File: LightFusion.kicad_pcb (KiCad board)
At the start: 4 copper layers, 52.3 x 52.3 mm, 100 parts, among them J1 303C-C4115-30-04, J2 TC2030-IDC-FP, P1 PHR-2, U1 MDBT42-512KV2, U10 OPA381AIDGKR, U2 TPS7A2033PDBVR, U3 TPS22918DBVR, U4 DRV8837DSGR, U5 ADS1292IPBSR, U6 STCS1APHR_FIXED, U7 STCS1APHR_FIXED, U8 TMP1075NDRLR, U9 MCP3561T-E_ST

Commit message: new rect version
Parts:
- removed C30, C31: 10 nF, LightFusion:C_0603_1608Metric
- added OPT1: FP11055_LISA2-RS-PIN, LightFusion:LEDIL_FP11055_LISA2_RS_PIN, F.Cu at (141.9, 130.2)
- added OPT2: FP11055_LISA2-RS-PIN, LightFusion:LEDIL_FP11055_LISA2_RS_PIN, F.Cu at (154.0, 130.2)
- added R36: 100k, LightFusion:R_0603_1608Metric, F.Cu at (154.1, 125.6)
- added R37: 100k, LightFusion:R_1206_3216Metric, F.Cu at (134.3, 125.0)
- C26, C28: value 4.7 uF -> 10 uF
- E1, E2, E3, E4, E5: footprint LightFusion:MILL-MAX_0906-0-15-20-76-14-11-0 -> LightFusion:0914015207714110
- J2: footprint LightFusion:TC2030IDCNL -> LightFusion:TC2030IDCFP
- U3: footprint LightFusion:TPS22918DBVR-6N -> LightFusion:TPS22918DBVT
- U6, U7: value STCS1APHR_FIXED -> ~; footprint LightFusion:STCS1APHR-8_STM -> LightFusion:PAM2808BLBR
- moved R25 1.55 mm to (135.1, 121.0)
- moved C26 0.18 mm to (127.3, 132.0)
- moved J2 0.15 mm to (137.9, 147.1)
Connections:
- D1 pad 1: /LED/LED730_K -> Net-(D1-K)
- D1 pad 2: VBAT_SYSTEM -> Net-(D1-A)
- D2 pad 1: /LED/LED850_K -> Net-(D2-K)
- D2 pad 2: VBAT_SYSTEM -> Net-(D2-A)
- R25 pad 1: Net-(U6-FB) -> Net-(D1-K)
- R26 pad 1: Net-(U7-FB) -> Net-(D2-K)
- U6 pad 1: VBAT_SYSTEM -> unconnected-(U6-NC-Pad1)
- U6 pad 2: PWM_730 -> VBAT_SYSTEM
- U6 pad 3: 3V3_DIG -> PWM_730
- U6 pad 4: /LED/LED730_K -> GND
- U6 pad 5: Net-(U6-FB) -> unconnected-(U6-NC-Pad5)
- U6 pad 6: GND -> Net-(D1-K)
- U6 pad 7: Net-(U6-SLOPE) -> Net-(D1-A)
- U7 pad 1: VBAT_SYSTEM -> unconnected-(U7-NC-Pad1)
- U7 pad 2: PWM_850 -> VBAT_SYSTEM
- U7 pad 3: 3V3_DIG -> PWM_850
- U7 pad 4: /LED/LED850_K -> GND
- U7 pad 5: Net-(U7-FB) -> unconnected-(U7-NC-Pad5)
- U7 pad 6: GND -> Net-(D2-K)
- U7 pad 7: Net-(U7-SLOPE) -> Net-(D2-A)
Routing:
- net 3V3_DIG: track 174.2 -> 0.00 mm, vias 19 -> 0
- net GND: track 130.1 -> 0.00 mm, vias 70 -> 0
- net VBAT_SYSTEM: track 110.3 -> 0.00 mm, vias 5 -> 0
- net /SWDIO: track 84.8 -> 0.00 mm, vias 2 -> 0
- net /SWDCLK: track 83.5 -> 0.00 mm, vias 4 -> 0
- net /RESET: track 79.4 -> 0.00 mm, vias 2 -> 0
- net ADC_MOSI: track 56.7 -> 0.00 mm, vias 4 -> 0
- net /MCU_STIM_IN2: track 55.8 -> 0.00 mm, vias 2 -> 0
- net ADC_MISO: track 54.4 -> 0.00 mm, vias 3 -> 0
- net ADC_SCK: track 54.4 -> 0.00 mm, vias 4 -> 0
- net /MCU_STIM_IN1: track 50.0 -> 0.00 mm, vias 2 -> 0
- net PWM_730: track 44.2 -> 0.00 mm
- net ADC_DRDY_N: track 41.3 -> 0.00 mm, vias 2 -> 0
- net /PD_ADC/3V3_A: track 40.5 -> 0.00 mm, vias 2 -> 0
- net /MCU_STIM_EN: track 40.3 -> 0.00 mm, vias 2 -> 0
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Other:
- board size 52.3 x 52.3 mm -> 61 x 52.3 mm

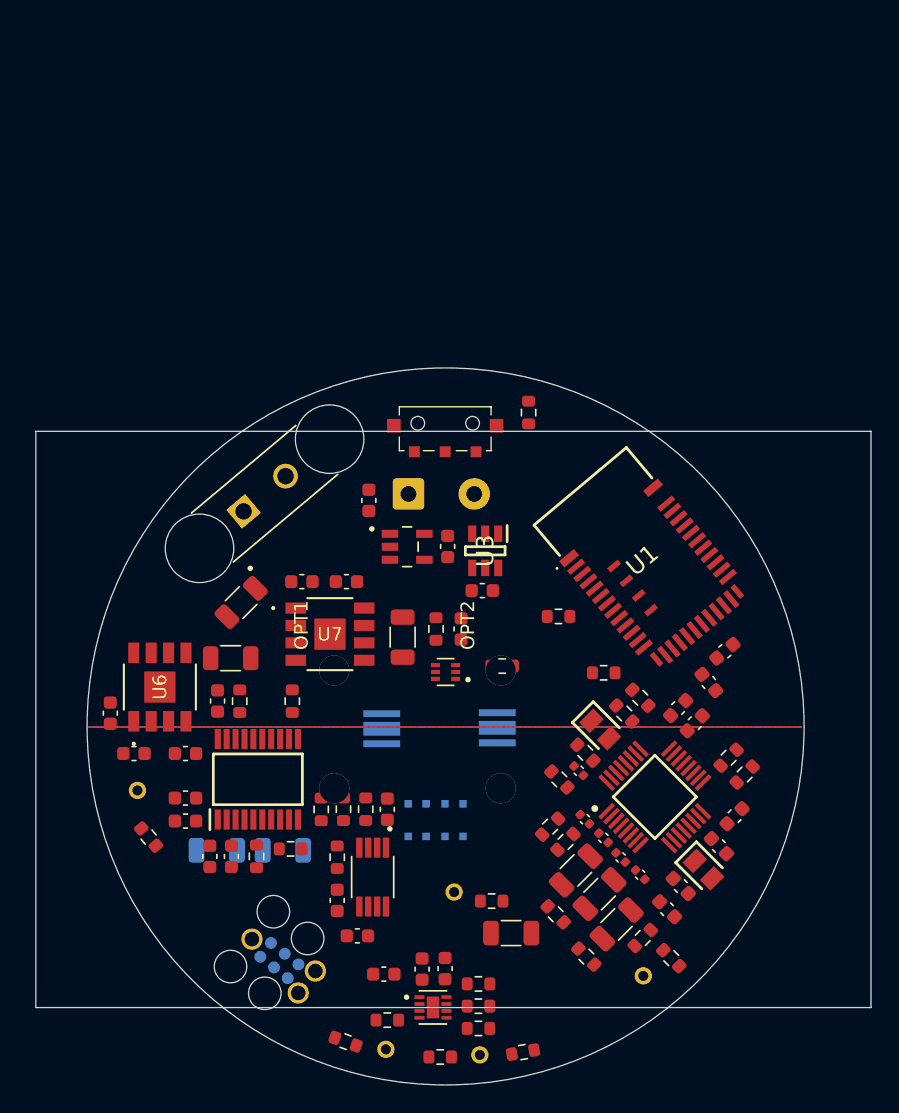
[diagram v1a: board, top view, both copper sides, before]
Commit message: rectangle placement
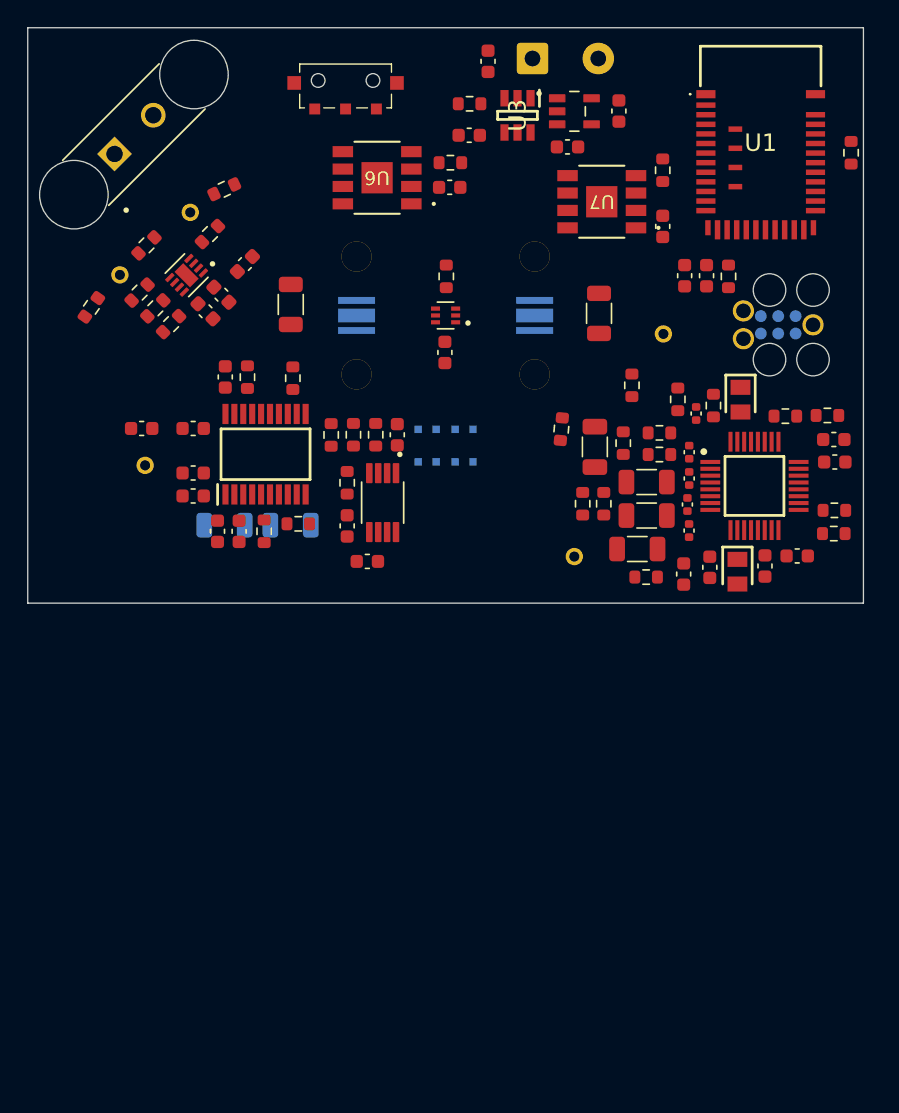
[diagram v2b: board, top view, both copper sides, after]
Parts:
- OPT1, OPT2: moved to B.Cu
- R37: footprint LightFusion:R_1206_3216Metric -> LightFusion:R_0603_1608Metric
- moved R21 63.0 mm to (128.2, 94.9), turned to 45 degrees
- moved R23 62.8 mm to (133.8, 90.8), turned to 25 degrees
- moved R22 62.8 mm to (124.1, 99.4), turned to -125 degrees
- moved E4 62.7 mm to (131.4, 92.5), turned to 45 degrees
- moved E5 62.7 mm to (126.2, 97.0), turned to 45 degrees
- moved R19 59.1 mm to (127.7, 98.3), turned to -135 degrees
- moved J2 59.0 mm to (174.3, 100.7), turned to 180 degrees
- moved R20 58.8 mm to (132.8, 94.1), turned to 45 degrees
- moved U4 56.4 mm to (131.1, 97.1), turned to -135 degrees
- moved R18 56.1 mm to (128.8, 99.5), turned to -135 degrees
- moved R17 53.1 mm to (130.0, 100.6), turned to 45 degrees
- moved C21 52.8 mm to (135.4, 96.2), turned to 45 degrees
- moved C22 51.4 mm to (133.6, 98.5), turned to -45 degrees
- moved C20 51.1 mm to (132.5, 99.7), turned to -45 degrees
- moved C27 45.7 mm to (150.3, 90.7), turned to 0 degrees
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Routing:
- removed copper zone on B.Cu, net GND
- removed copper zone on F.Cu, net GND
- removed copper zone on In1.Cu, net GND
- removed copper zone on In2.Cu, net GND
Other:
- board size 61 x 52.3 mm -> 61 x 42 mm

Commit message: fine allignment pcb
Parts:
- moved C39 1.15 mm to (133.4, 116.9)
- moved C40 1.15 mm to (134.9, 116.9)
- moved C42 1.15 mm to (142.8, 116.5)
- moved R28 1.15 mm to (135.5, 105.7)
- moved R30 1.15 mm to (139.2, 116.4)
- moved U9 1.15 mm to (136.9, 111.3)
- moved C26 1.15 mm to (127.8, 109.4)
- moved C33 1.15 mm to (131.6, 114.3)
- moved C34 1.15 mm to (131.6, 112.7)
- moved C35 1.15 mm to (131.6, 109.4)
- moved C36 1.15 mm to (133.9, 105.6)
- moved C37 1.15 mm to (138.7, 116.5)
- moved C38 1.15 mm to (133.9, 116.5)
- moved C41 1.15 mm to (146.5, 109.9)
- moved C43 1.15 mm to (144.3, 119.1)
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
